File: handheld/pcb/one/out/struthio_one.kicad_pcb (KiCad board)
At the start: 2 copper layers, 83.8 x 104.3 mm, 7 parts, among them J1 Header_2x16_Waveshare, J2 S2B-PH-K-S, SW1 TS-1187A-B-A-B, SW2 TS-1187A-B-A-B, SW3 TS-1187A-B-A-B, SW4 TS-1187A-B-A-B, SW5 SS-12D06-G030

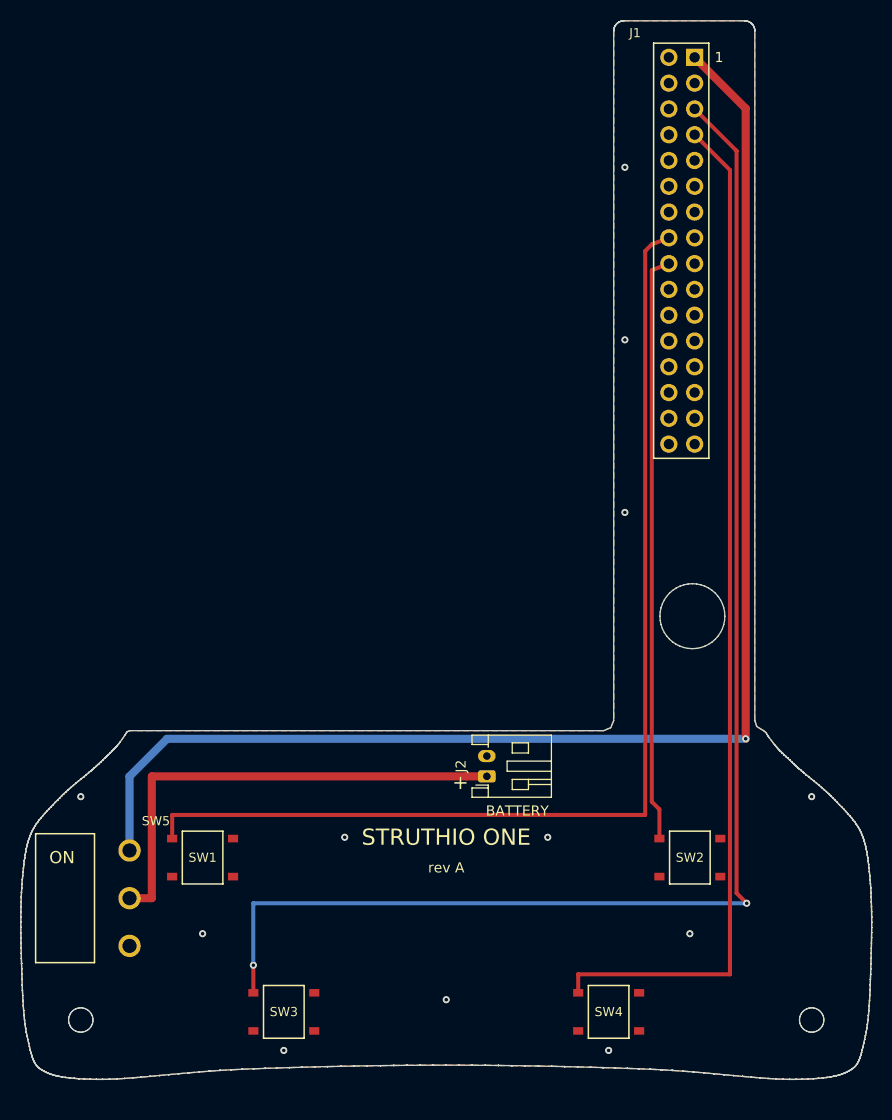
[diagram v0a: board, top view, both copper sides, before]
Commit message: STRUTHIO ONE: round wing buttons, 74 mm controller, BOTH badge; dart defaults to ROCKER ONLY
Wing buttons are now 16 mm round caps at x +-18 with a wing engraved on top
(left flaps up-left, right up-right, both together straight up). The rocker
below stays for the aim-assisted dart. With round caps the controller only
flares to 74 mm (was 88). The face panel art adds orange/blue rings round
each button and a BOTH straight-up badge between them; the rocker bay now
runs out of the bottom edge with straight sides, and the panel outline has
no slivers. Board-locating ribs, lower screws and plate posts moved inward.

ONE board rev B: the wing switches follow the buttons; GPIO17 now crosses
under the right button on the bottom layer. KiCad DRC: no errors, no
unconnected pads. Gerbers, BOM and CPL regenerated.

Firmware: the default DART mode is ROCKER ONLY, so holding both wings means
straight up and never a dart (mode C stays selectable for a rocker-less
bench board). Real ESP-IDF build OK; host tests pass.

Co-Authored-By: Claude Opus 5.5 <noreply@anthropic.com>
Claude-Session: https://claude.ai/code/session_01BN2x2AjDXTm5ZbuwkUnxX5
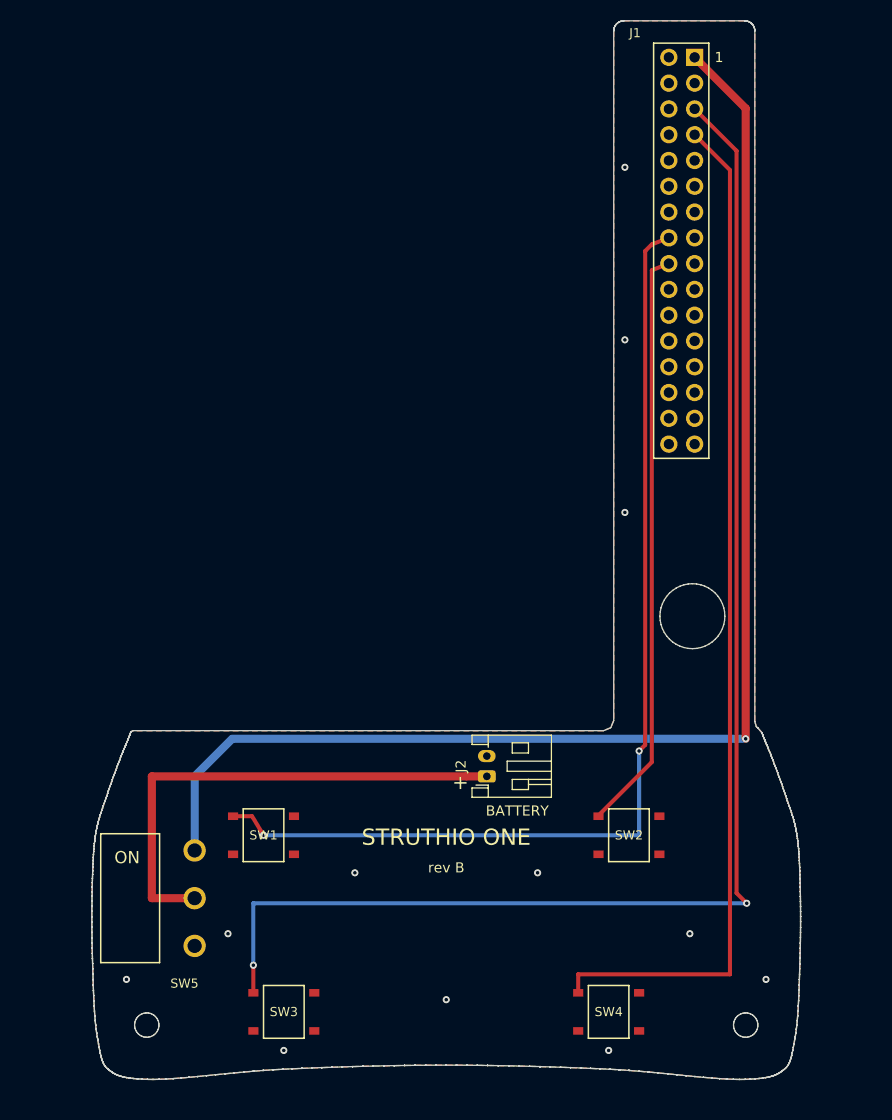
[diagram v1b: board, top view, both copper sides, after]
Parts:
- moved SW5 6.41 mm to (75.2, 150.0)
- moved SW1 6.39 mm to (82.0, 143.8)
- moved SW2 6.39 mm to (118.0, 143.8)
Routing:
- net BAT: track 138.7 -> 132.3 mm
- net GPIO17: track 107.2 -> 101.6 mm, vias 0 -> 2
- net BAT_RAW: track 47.2 -> 49.2 mm
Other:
- board size 83.8 x 104.3 mm -> 69.8 x 104.3 mm
- board text added: "rev B"
- board text removed: "rev A"

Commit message: STRUTHIO ONE: no thin parts on the face
Measured: the panel strip between the wing wells and the rocker was 2.7 mm,
the open rocker bay left thin legs, and the printed face below the rocker was
2.45 mm (mostly edge round-over). Now: wing buttons up 2.7 mm, rocker 7.2 mm
tall (was 9) at y -59, the bottom edge straight (was 1.4 mm concave), the
rocker well closed in the panel. Panel: nothing narrower than 3 mm, 3.5 mm
between the wells, 3.4 mm under the rocker. Shell: 6.95 mm of face below the
rocker. New checks guard all three (57 checks pass).

Board: battery socket and rocker routes follow; DRC no errors, no
unconnected pads; Gerbers, BOM, CPL regenerated.

Co-Authored-By: Claude Opus 5.5 <noreply@anthropic.com>
Claude-Session: https://claude.ai/code/session_01BN2x2AjDXTm5ZbuwkUnxX5
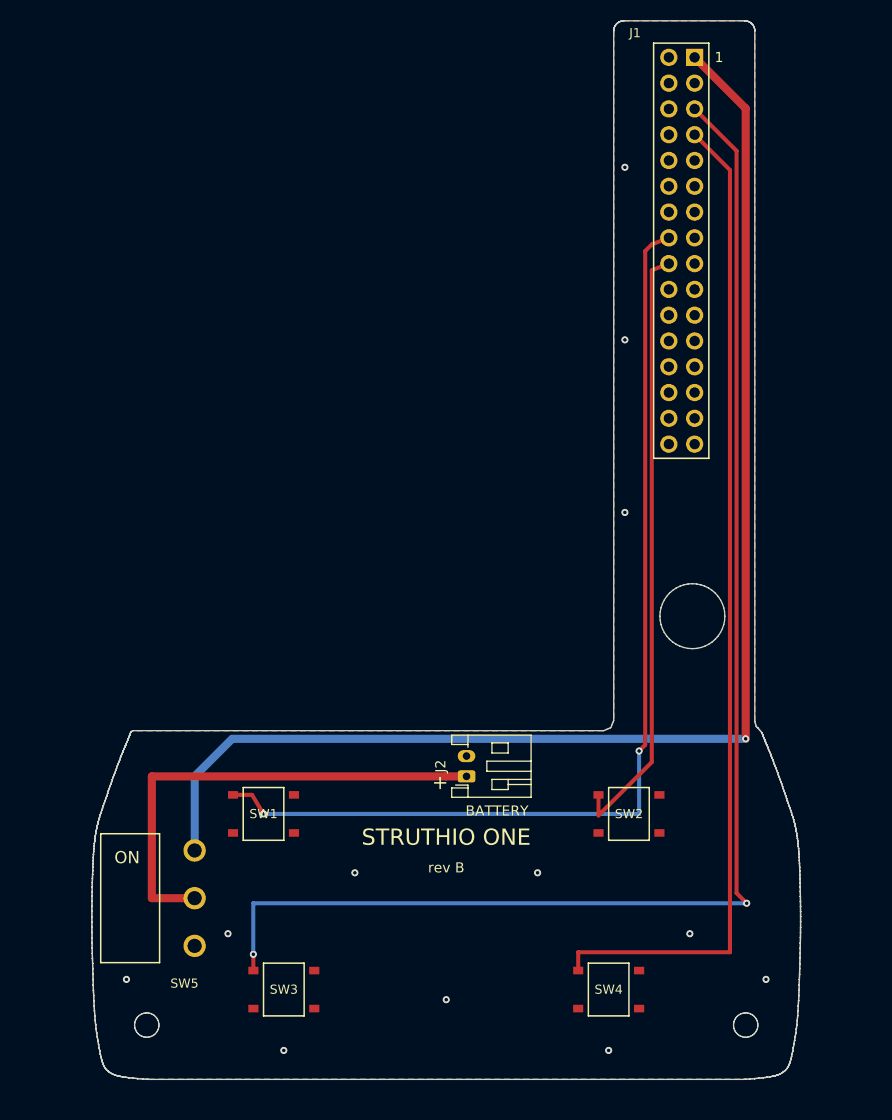
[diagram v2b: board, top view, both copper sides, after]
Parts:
- moved SW3 2.20 mm to (84.0, 159.0)
- moved SW4 2.20 mm to (116.0, 159.0)
- moved SW1 2.10 mm to (82.0, 141.7)
- moved SW2 2.10 mm to (118.0, 141.7)
- moved J2 2.00 mm to (102.0, 138.0)
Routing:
- net GPIO38: track 100.9 -> 98.7 mm
- net GPIO21: track 137.8 -> 135.6 mm
- net GPIO17: track 101.6 -> 99.5 mm
- net BAT_RAW: track 49.2 -> 47.2 mm
- net GPIO18: track 57.8 -> 59.7 mm
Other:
- outline, holes or cut-outs redrawn

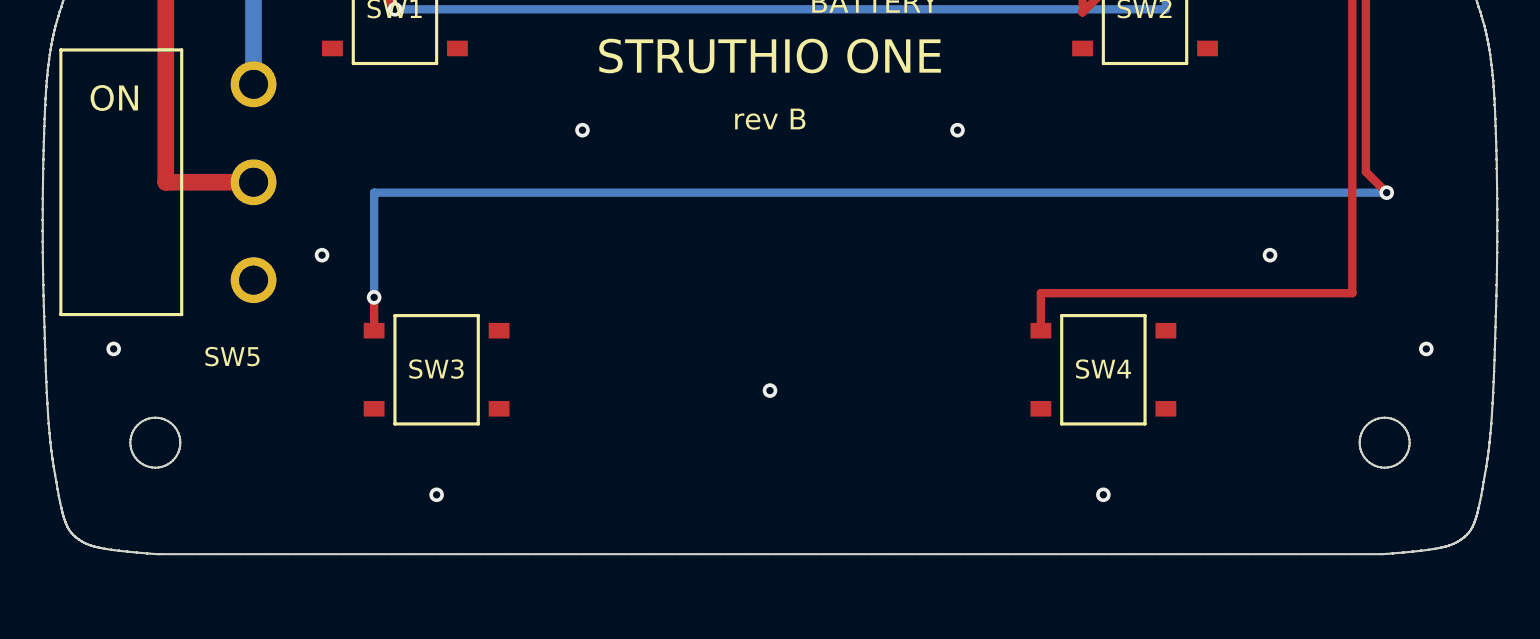
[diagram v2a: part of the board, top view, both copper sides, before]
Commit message: STRUTHIO ONE: scooped bottom back, body 2 mm longer (136 mm)
The gently concave bottom edge returns, and the body grows 2 mm downward to
pay for it: at the shallowest point under the rocker the printed face is now
7.55 mm (was 6.95 flat, 2.45 originally) and the panel strip under the rocker
well is 4.0 mm. The lip check now measures under the rocker, not at the
lowest corner. Controls unchanged. Board outline, Gerbers, panel files and
renders regenerated; 57 CAD checks pass; DRC clean.

Co-Authored-By: Claude Opus 5.5 <noreply@anthropic.com>
Claude-Session: https://claude.ai/code/session_01BN2x2AjDXTm5ZbuwkUnxX5
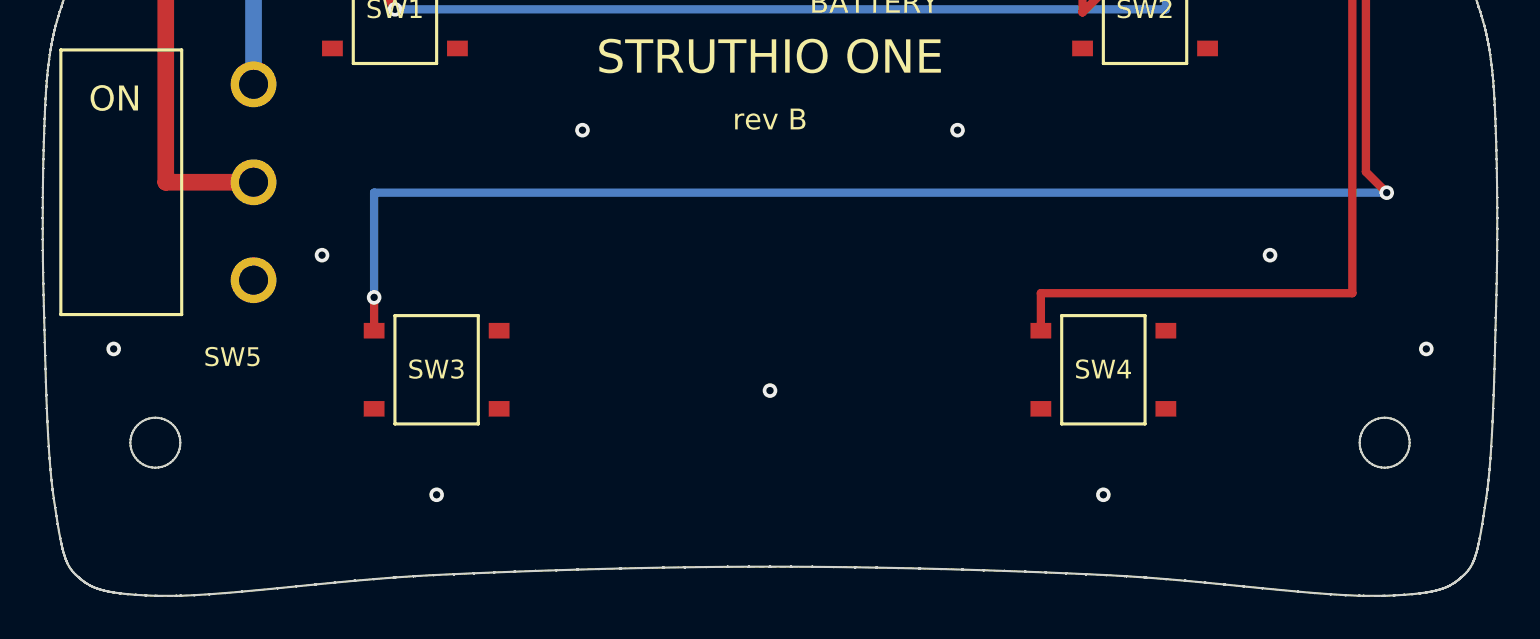
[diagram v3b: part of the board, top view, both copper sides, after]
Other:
- board size 69.8 x 104.3 mm -> 69.8 x 106.3 mm

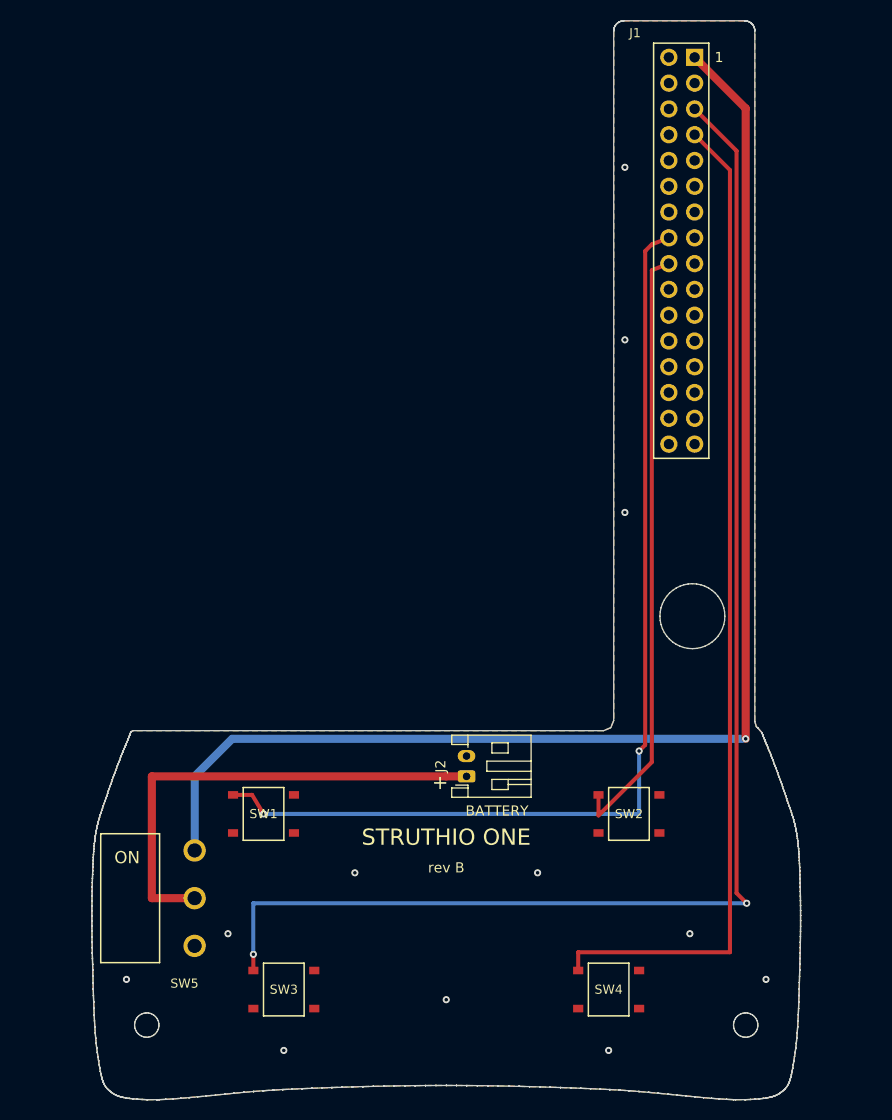
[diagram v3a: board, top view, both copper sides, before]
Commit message: STRUTHIO ONE hardware debug: header, mounting, power-on, reverse battery, slide switch
Walking the build against the manufacturers' data found five real problems:

1. J1 header: LCSC lists PZ254-2-16-Z-8.5 as 6 mm mating / 3 mm tail. JLC fits it
   the standard way, so 'long pins through' could not be relied on. Now mounted
   standard; the ONE board rests on the front bosses so the 6 mm pins go 3.3 mm
   into the ~4 mm J8 socket (Z_ONE 18.54). Board inset 0.8 mm more and the strip
   narrowed to clear the back shell's inner round-over; right lanes re-spaced.
2. Waveshare mounting: nothing confirms a thread in its M2 holes (Waveshare ships
   only the board and speaker). No screws into it now: three back-shell posts
   with pegs locate it, a 3 mm foam pad behind the battery clamps battery and
   board; 2 screws total. Screw heads now sunk flush (they would have stood
   0.7 mm proud with the deeper stack).
3. Power-on: AXP2101 datasheet 6.5.2 - on battery alone the battery switch stays
   off until PWR is held (ONLEVEL up to 2 s by eFuse). The slide switch alone
   would never start it. ONE board rev C adds Q2 AO3400A + C1 10uF + R1 470k +
   D1 1N4148WS: PWR (header pin 24) held low ~3-8 s whenever the switch turns on.
   Firmware disables long-press power-off at every boot.
4. Reverse battery: JST PH leads come wired both ways; Q1 AO3401A in the battery
   line switches off for a reversed lead. All five new parts are JLC basic.
5. SS-12D06-G030 drawing: pin centre 3.75 mm behind the body (was 3.45); holes
   1.6 mm for the 0.7 x 1.3 mm pins. ON = knob toward the screen.

60 CAD checks pass; KiCad DRC no errors, no unconnected pads; real ESP-IDF
build OK; handheld checks pass.

Co-Authored-By: Claude Opus 5.5 <noreply@anthropic.com>
Claude-Session: https://claude.ai/code/session_01BN2x2AjDXTm5ZbuwkUnxX5
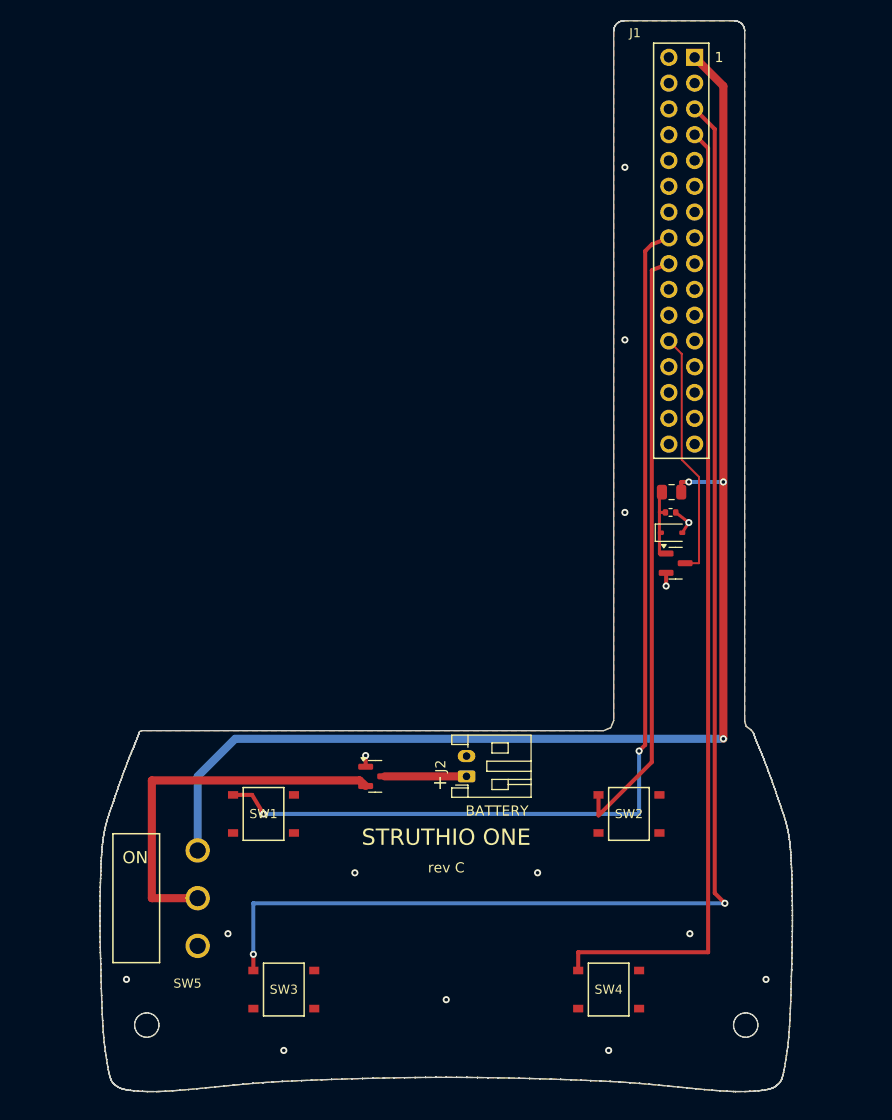
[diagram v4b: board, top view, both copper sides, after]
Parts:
- added C1: 10uF, C_0805_2012Metric, F.Cu at (122.2, 110.0)
- added D1: 1N4148WS, D_SOD-323, F.Cu at (122.2, 114.0)
- added Q1: AO3401A, SOT-23, F.Cu at (93.0, 138.0)
- added Q2: AO3400A, SOT-23, F.Cu at (122.6, 117.0)
- added R1: 470k, R_0402_1005Metric, F.Cu at (122.1, 112.0)
- moved SW5 0.30 mm to (75.5, 150.0)
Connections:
- J1 pad 24: (no net) -> PWRON
- J2 pad 1: BAT_RAW -> BAT_IN
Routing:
- net PWRON: track 0.00 -> 24.5 mm
- net BAT_RAW: track 47.2 -> 37.4 mm
- net BAT_IN: track 0.00 -> 8.06 mm
- net PG: track 0.00 -> 7.70 mm
- net GND: track 0.00 -> 5.22 mm, vias 12 -> 15
- net GPIO38: track 98.7 -> 95.7 mm
- net GPIO21: track 135.6 -> 132.6 mm
- net BAT: track 132.3 -> 134.1 mm, vias 1 -> 3
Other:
- board size 69.8 x 106.3 mm -> 68.2 x 105.5 mm
- board text added: "rev C"
- board text removed: "J1: LONG PINS THROUGH THIS BOARD"
- board text removed: "rev B"
